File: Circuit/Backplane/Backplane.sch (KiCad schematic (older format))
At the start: 51 parts

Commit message: fixground
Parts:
- removed R?: 4.7K, symbol R
- added R?: 4.7K, symbol R
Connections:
- net GND: now also R?.2
- net at U?.17 (TEST): now also R?.1
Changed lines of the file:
@@
 $EndDescr
-$Comp
-L TUSB4041I U?
-U 1 1 5A564068
-P 4400 4650
-F 0 "U?" H 5000 6750 50  0000 L CNN
-F 1 "TUSB4041I" H 5000 6650 50  0000 L CNN
-F 2 "Housings_QFP:HTQFP-64_1EP_10x10mm_Pitch0.5mm_ThermalPad" H 5600 6650 50  0001 L CNN
-F 3 "" H 4100 4850 50  0001 C CNN
-	1    4400 4650
-	1    0    0    -1
-$EndComp
 $Comp
 L Conn-PCIE-x1 CON?
@@
 $EndComp
 $Comp
-L R R?
-U 1 1 5A56456F
-P 2550 6700
-F 0 "R?" V 2630 6700 50  0000 C CNN
-F 1 "4.7K" V 2550 6700 50  0000 C CNN
-F 2 "" V 2480 6700 50  0001 C CNN
-F 3 "" H 2550 6700 50  0001 C CNN
-	1    2550 6700
-	1    0    0    -1
-$EndComp
-$Comp
-L GND #PWR?
-U 1 1 5A564784
-P 3250 6900
-F 0 "#PWR?" H 3250 6650 50  0001 C CNN
-F 1 "GND" H 3250 6750 50  0000 C CNN
-F 2 "" H 3250 6900 50  0001 C CNN
-F 3 "" H 3250 6900 50  0001 C CNN
-	1    3250 6900
-	1    0    0    -1
-$EndComp
-$Comp
 L USB_OTG J?
 U 1 1 5A564864
@@
 	7250 5850 6700 5850
 Wire Wire Line
-	4400 6900 4400 6750
-Connection ~ 3250 6900
-Wire Wire Line
 	2100 3550 2950 3550
 Wire Wire Line
@@
 Wire Wire Line
 	1950 6250 3100 6250
-Wire Wire Line
-	3100 6450 2550 6450
-Wire Wire Line
-	2550 6450 2550 6550
-Wire Wire Line
-	2550 6850 2550 6900
-Connection ~ 2550 6900
 $Comp
 L R R?
@@
 	1    0    0    -1
 $EndComp
-Wire Wire Line
-	2550 6900 4400 6900
+$Comp
+L R R?
+U 1 1 5A6197DD
+P 2850 6450
+F 0 "R?" V 2930 6450 50  0000 C CNN
+F 1 "4.7K" V 2850 6450 50  0000 C CNN
+F 2 "" V 2780 6450 50  0001 C CNN
+F 3 "" H 2850 6450 50  0001 C CNN
+	1    2850 6450
+	0    1    1    0
+$EndComp
+Wire Wire Line
+	3100 6450 3000 6450
+Wire Wire Line
+	2700 6450 2700 6750
+$Comp
+L GND #PWR?
+U 1 1 5A619BE9
+P 3500 6750
+F 0 "#PWR?" H 3500 6500 50  0001 C CNN
+F 1 "GND" H 3500 6600 50  0000 C CNN
+F 2 "" H 3500 6750 50  0001 C CNN
+F 3 "" H 3500 6750 50  0001 C CNN
+	1    3500 6750
+	1    0    0    -1
+$EndComp
+$Comp
+L TUSB4041I U?
+U 1 1 5A564068
+P 4400 4650
+F 0 "U?" H 5000 6750 50  0000 L CNN
+F 1 "TUSB4041I" H 5000 6650 50  0000 L CNN
+F 2 "Housings_QFP:HTQFP-64_1EP_10x10mm_Pitch0.5mm_ThermalPad" H 5600 6650 50  0001 L CNN
+F 3 "" H 4100 4850 50  0001 C CNN
+	1    4400 4650
+	1    0    0    -1
+$EndComp
+Wire Wire Line
+	2700 6750 4400 6750
+Connection ~ 3500 6750
 $EndSCHEMATC

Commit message: PcieFix
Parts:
- removed P?: InnerPoe, symbol XT30
- CON?: value Conn-PCIE-x1 -> Power_dist
- CON?: value Conn-PCIE-x1 -> Peripheral_bridge
- J?: value PressureSensor -> Pneumatic
- P?: value General1 -> Computer1
- P?: value General2 -> Computer2
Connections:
- net 12V: no longer CON?.A3 (V12), P?.1 (P1), P?.1 (P1)
- net GND: no longer CON?.B7 (GND), J?.1 (Pin_1)
- net VPCIE: now also P?.1 (P1)
- net at CON?.A7 (JTAG_TDO): no longer J?.2 (Pin_2)
- net at CON?.A8 (JTAG_TMS): no longer J?.3 (Pin_3)
- net Vin: no longer names the net of C?.1, CON?.A10 (VCC3), CON?.A9 (VCC3), CON?.B8 (VCC3), L?.1
- new net GND_Vbatt: CON?.B7 (GND)
- new net Vbatt: CON?.A3 (V12), P?.1 (P1)
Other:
- moved on the sheet: J?
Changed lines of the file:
@@
 P 7400 1550
 F 0 "CON?" H 7550 1600 60  0000 C CNN
-F 1 "Conn-PCIE-x1" H 7800 -550 60  0000 C CNN
+F 1 "Power_dist" H 7800 -550 60  0000 C CNN
 F 2 "" H 7400 1550 60  0001 C CNN
 F 3 "" H 7400 1550 60  0001 C CNN
@@
 P 7450 4250
 F 0 "CON?" H 7600 4300 60  0000 C CNN
-F 1 "Conn-PCIE-x1" H 7850 2150 60  0000 C CNN
+F 1 "Peripheral_bridge" H 7850 2150 60  0000 C CNN
 F 2 "" H 7450 4250 60  0001 C CNN
 F 3 "" H 7450 4250 60  0001 C CNN
@@
 Text GLabel 8500 4500 2    60   Input ~ 0
 12V
-Text GLabel 8450 1800 2    60   Input ~ 0
-12V
 $Comp
 L C C?
@@
 Text GLabel 8450 2500 2    60   Input ~ 0
 VPCIE
-Text GLabel 7150 5050 0    60   Input ~ 0
-Vin
-Text GLabel 8500 5200 2    60   Input ~ 0
-Vin
 $Comp
 L C C?
@@
 Text GLabel 5750 5050 0    60   Input ~ 0
 5V
-Text GLabel 6450 5050 2    60   Input ~ 0
-Vin
-$Comp
-L XT30 P?
-U 1 1 5A58183A
-P 10450 2000
-F 0 "P?" H 10450 2150 50  0000 C CNN
-F 1 "InnerPoe" H 10450 1850 50  0000 C CNN
-F 2 "" H 10450 2000 60  0000 C CNN
-F 3 "" H 10450 2000 60  0000 C CNN
-	1    10450 2000
-	1    0    0    -1
-$EndComp
 $Comp
 L XT30 P?
@@
 P 10450 3200
 F 0 "P?" H 10450 3350 50  0000 C CNN
-F 1 "General1" H 10450 3050 50  0000 C CNN
+F 1 "Computer1" H 10450 3050 50  0000 C CNN
 F 2 "" H 10450 3200 60  0000 C CNN
 F 3 "" H 10450 3200 60  0000 C CNN
@@
 P 10450 3600
 F 0 "P?" H 10450 3750 50  0000 C CNN
-F 1 "General2" H 10450 3450 50  0000 C CNN
+F 1 "Computer2" H 10450 3450 50  0000 C CNN
 F 2 "" H 10450 3600 60  0000 C CNN
 F 3 "" H 10450 3600 60  0000 C CNN
 	1    10450 3600
-	1    0    0    -1
-$EndComp
-$Comp
-L GND #PWR?
-U 1 1 5A58301B
-P 10150 2100
-F 0 "#PWR?" H 10150 1850 50  0001 C CNN
-F 1 "GND" H 10150 1950 50  0000 C CNN
-F 2 "" H 10150 2100 50  0001 C CNN
-F 3 "" H 10150 2100 50  0001 C CNN
-	1    10150 2100
 	1    0    0    -1
 $EndComp
@@
 	1    0    0    -1
 $EndComp
-Text GLabel 10150 1950 0    60   Input ~ 0
-12V
-Text GLabel 10150 2350 0    60   Input ~ 0
-12V
 Text GLabel 10150 3150 0    60   Input ~ 0
 12V
@@
 L Conn_01x03 J?
 U 1 1 5A584C3E
-P 9550 2050
-F 0 "J?" H 9550 2250 50  0000 C CNN
-F 1 "Rs232DVL" H 9550 1850 50  0000 C CNN
-F 2 "" H 9550 2050 50  0001 C CNN
-F 3 "" H 9550 2050 50  0001 C CNN
-	1    9550 2050
-	1    0    0    -1
-$EndComp
-Text GLabel 10150 2750 0    60   Input ~ 0
-12V
+P 9550 4250
+F 0 "J?" H 9550 4450 50  0000 C CNN
+F 1 "Rs232DVL" H 9550 4050 50  0000 C CNN
+F 2 "" H 9550 4250 50  0001 C CNN
+F 3 "" H 9550 4250 50  0001 C CNN
+	1    9550 4250
+	1    0    0    -1
+$EndComp
 $Comp
 L Conn_01x03 J?
@@
 Connection ~ 7200 1750
 Wire Wire Line
-	8350 1750 8350 1850
-Wire Wire Line
 	7200 1950 7150 1950
 Wire Wire Line
 	7150 1950 7150 3700
 Wire Wire Line
-	7150 2250 7200 2250
-Wire Wire Line
 	7150 2950 7200 2950
-Connection ~ 7150 2250
 Wire Wire Line
 	7150 3250 7200 3250
@@
 	7150 3450 7200 3450
 Connection ~ 7150 3250
-Wire Wire Line
-	8350 1950 9350 1950
 Wire Wire Line
 	8400 2850 8350 2850
@@
 	7200 1750 7100 1750
 Wire Wire Line
-	8350 1800 8450 1800
-Connection ~ 8350 1800
-Wire Wire Line
 	7250 4450 7150 4450
 Wire Wire Line
@@
 Connection ~ 6550 2550
 Wire Wire Line
-	7250 5050 7150 5050
+	6050 5050 7250 5050
 Wire Wire Line
 	8400 5150 8400 5250
-Wire Wire Line
-	8400 5200 8500 5200
-Connection ~ 8400 5200
 Connection ~ 6300 5050
 Wire Wire Line
@@
 	7150 3700 8400 3700
 Wire Wire Line
-	10250 1950 10150 1950
-Wire Wire Line
-	10250 2050 10150 2050
-Wire Wire Line
-	10150 2050 10150 2100
-Wire Wire Line
 	10250 2350 10150 2350
 Wire Wire Line
@@
 Wire Wire Line
 	10150 3650 10150 3700
-Connection ~ 8400 1950
-Wire Wire Line
-	8350 2250 8450 2250
-Wire Wire Line
-	8450 2250 8450 2050
-Wire Wire Line
-	8450 2050 9350 2050
-Wire Wire Line
-	8500 2150 9350 2150
-Wire Wire Line
-	8500 2150 8500 2350
-Wire Wire Line
-	8500 2350 8350 2350
 Wire Wire Line
 	6850 4950 7250 4950
@@
 	0    1    1    0
 $EndComp
-Wire Wire Line
-	6050 5050 6450 5050
 $Comp
 L Ferrite_Bead L?
@@
 P 9600 5400
 F 0 "J?" H 9650 5600 50  0000 C CNN
-F 1 "PressureSensor" H 9650 5100 50  0000 C CNN
+F 1 "Pneumatic" H 9650 5100 50  0000 C CNN
 F 2 "" H 9600 5400 50  0001 C CNN
 F 3 "" H 9600 5400 50  0001 C CNN
@@
 	2700 6750 4400 6750
 Connection ~ 3500 6750
+Wire Wire Line
+	8350 1750 8500 1750
+Wire Wire Line
+	8500 1750 8500 1650
+Wire Wire Line
+	8500 1650 8650 1650
+Wire Wire Line
+	8350 1850 8650 1850
+Text GLabel 8650 1650 2    60   Input ~ 0
+12V
+Text GLabel 8650 1850 2    60   Input ~ 0
+Vbatt
+Wire Wire Line
+	7200 2250 6800 2250
+Wire Wire Line
+	6800 2250 6800 1450
+Wire Wire Line
+	6800 1450 6850 1450
+Text GLabel 6850 1450 2    60   Input ~ 0
+GND_Vbatt
+Text GLabel 10150 2350 0    60   Input ~ 0
+VPCIE
+Text GLabel 10150 2750 0    60   Input ~ 0
+Vbatt
+Wire Wire Line
+	8400 1950 8350 1950
+Wire Wire Line
+	8400 5200 8550 5200
+Wire Wire Line
+	8550 5200 8550 6600
+Wire Wire Line
+	8550 6600 6550 6600
+Wire Wire Line
+	6550 6600 6550 5050
+Connection ~ 6550 5050
+Connection ~ 8400 5200
 $EndSCHEMATC

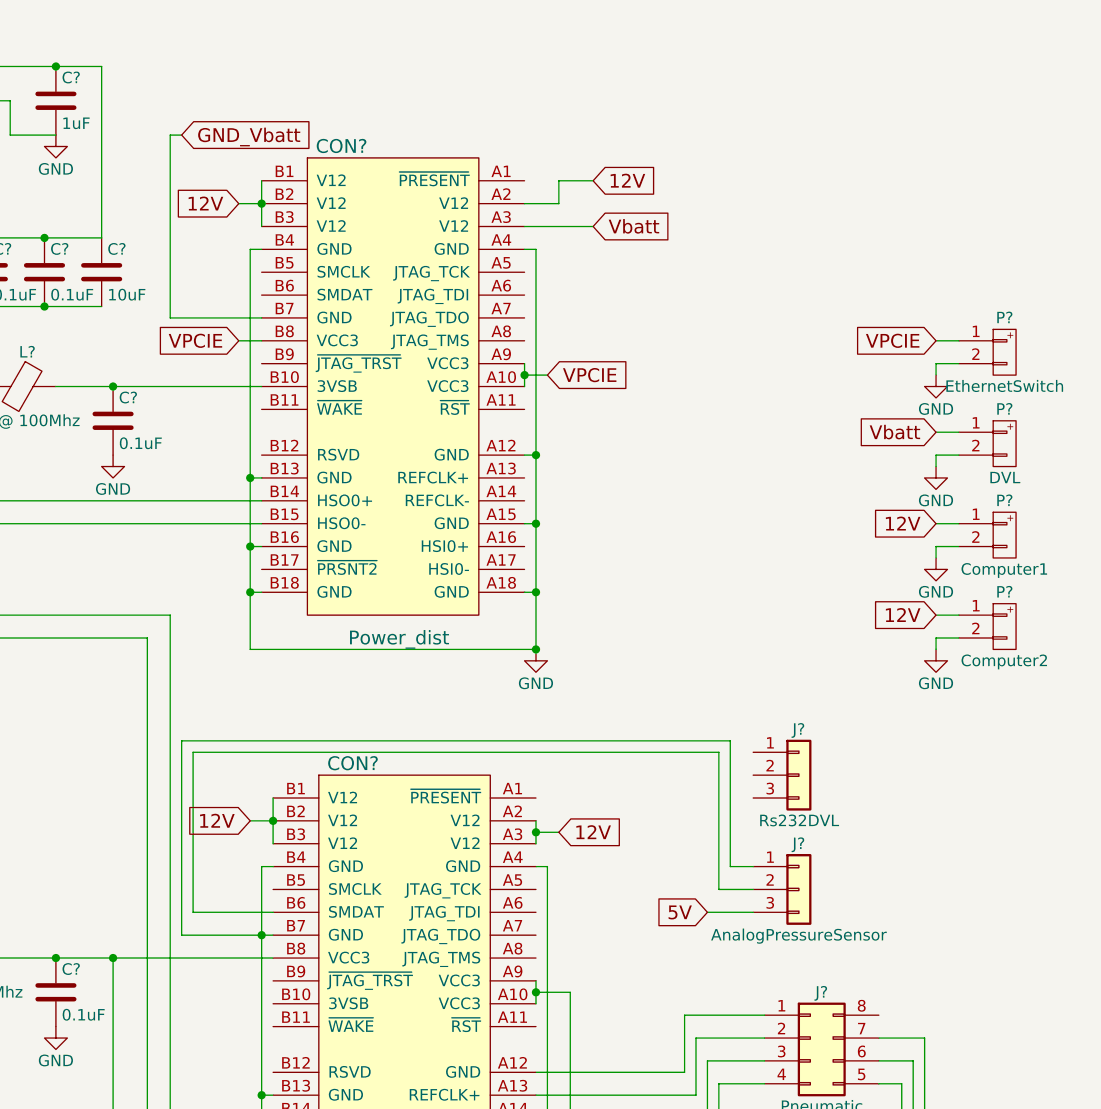
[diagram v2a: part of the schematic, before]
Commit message: fixDv,Change_label_to_powerflag
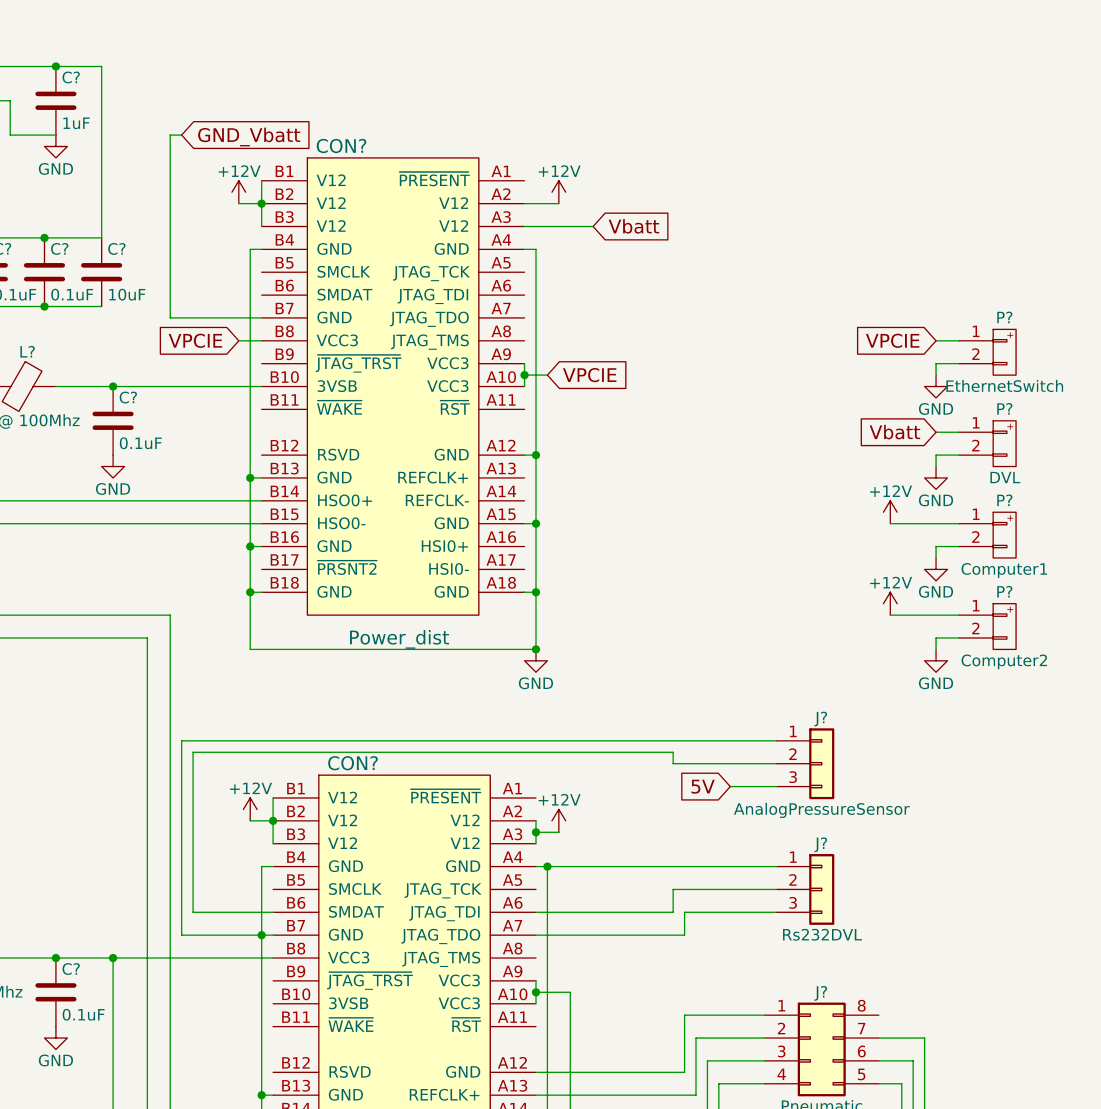
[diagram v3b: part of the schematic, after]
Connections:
- net GND: now also J?.1 (Pin_1)
- net at CON?.A6 (JTAG_TDI): now also J?.2 (Pin_2)
- net at CON?.A7 (JTAG_TDO): now also J?.3 (Pin_3)
- net 12V renamed +12V
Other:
- moved on the sheet: J?
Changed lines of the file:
@@
 	1    0    0    -1
 $EndComp
-Text GLabel 7100 1750 0    60   Input ~ 0
-12V
-Text GLabel 7150 4450 0    60   Input ~ 0
-12V
-Text GLabel 8500 4500 2    60   Input ~ 0
-12V
 $Comp
 L C C?
@@
 	1    0    0    -1
 $EndComp
-Text GLabel 10150 3150 0    60   Input ~ 0
-12V
-Text GLabel 10150 3550 0    60   Input ~ 0
-12V
 $Comp
 L Conn_01x03 J?
 U 1 1 5A584C3E
-P 9550 4250
-F 0 "J?" H 9550 4450 50  0000 C CNN
-F 1 "Rs232DVL" H 9550 4050 50  0000 C CNN
-F 2 "" H 9550 4250 50  0001 C CNN
-F 3 "" H 9550 4250 50  0001 C CNN
-	1    9550 4250
+P 9650 4750
+F 0 "J?" H 9650 4950 50  0000 C CNN
+F 1 "Rs232DVL" H 9650 4550 50  0000 C CNN
+F 2 "" H 9650 4750 50  0001 C CNN
+F 3 "" H 9650 4750 50  0001 C CNN
+	1    9650 4750
 	1    0    0    -1
 $EndComp
@@
 L Conn_01x03 J?
 U 1 1 5A5725F7
-P 9550 4750
-F 0 "J?" H 9550 4950 50  0000 C CNN
-F 1 "AnalogPressureSensor" H 9550 4550 50  0000 C CNN
-F 2 "" H 9550 4750 50  0001 C CNN
-F 3 "" H 9550 4750 50  0001 C CNN
-	1    9550 4750
-	1    0    0    -1
-$EndComp
-Text GLabel 9150 4850 0    60   Input ~ 0
+P 9650 4200
+F 0 "J?" H 9650 4400 50  0000 C CNN
+F 1 "AnalogPressureSensor" H 9650 4000 50  0000 C CNN
+F 2 "" H 9650 4200 50  0001 C CNN
+F 3 "" H 9650 4200 50  0001 C CNN
+	1    9650 4200
+	1    0    0    -1
+$EndComp
+Text GLabel 9250 4300 0    60   Input ~ 0
 5V
 $Comp
@@
 Connection ~ 7200 5950
 Wire Wire Line
-	8400 4650 8450 4650
+	8400 4650 9450 4650
 Wire Wire Line
 	8400 5550 9050 5550
@@
 	10150 2850 10150 2900
 Wire Wire Line
-	10250 3150 10150 3150
+	9950 3150 10250 3150
 Wire Wire Line
 	10250 3250 10150 3250
@@
 	10150 3250 10150 3300
 Wire Wire Line
-	10250 3550 10150 3550
+	9950 3550 10250 3550
 Wire Wire Line
 	10250 3650 10150 3650
@@
 	6850 4950 6850 4100
 Wire Wire Line
-	6850 4100 9250 4100
-Wire Wire Line
-	9250 4100 9250 4650
-Wire Wire Line
-	9250 4650 9350 4650
+	6850 4100 9450 4100
 Wire Wire Line
 	7250 4850 6900 4850
@@
 	6900 4850 6900 4150
 Wire Wire Line
-	6900 4150 9200 4150
-Wire Wire Line
-	9200 4150 9200 4750
-Wire Wire Line
-	9200 4750 9350 4750
-Wire Wire Line
-	9350 4850 9150 4850
+	9450 4300 9250 4300
 Wire Wire Line
 	8400 3700 8400 1950
@@
 	8350 1750 8500 1750
 Wire Wire Line
-	8500 1750 8500 1650
-Wire Wire Line
-	8500 1650 8650 1650
-Wire Wire Line
 	8350 1850 8650 1850
-Text GLabel 8650 1650 2    60   Input ~ 0
-12V
 Text GLabel 8650 1850 2    60   Input ~ 0
 Vbatt
@@
 Connection ~ 6550 5050
 Connection ~ 8400 5200
+Connection ~ 8450 4650
+Wire Wire Line
+	8400 4950 9050 4950
+Wire Wire Line
+	9050 4950 9050 4850
+Wire Wire Line
+	9050 4850 9450 4850
+Wire Wire Line
+	8400 4850 9000 4850
+Wire Wire Line
+	9000 4850 9000 4750
+Wire Wire Line
+	9000 4750 9450 4750
+Wire Wire Line
+	6900 4150 9000 4150
+Wire Wire Line
+	9000 4150 9000 4200
+Wire Wire Line
+	9000 4200 9450 4200
+$Comp
+L +12V #PWR?
+U 1 1 5A60ECE0
+P 7100 1750
+F 0 "#PWR?" H 7100 1600 50  0001 C CNN
+F 1 "+12V" H 7100 1890 50  0000 C CNN
+F 2 "" H 7100 1750 50  0001 C CNN
+F 3 "" H 7100 1750 50  0001 C CNN
+	1    7100 1750
+	1    0    0    -1
+$EndComp
+$Comp
+L +12V #PWR?
+U 1 1 5A60EF7F
+P 8500 1750
+F 0 "#PWR?" H 8500 1600 50  0001 C CNN
+F 1 "+12V" H 8500 1890 50  0000 C CNN
+F 2 "" H 8500 1750 50  0001 C CNN
+F 3 "" H 8500 1750 50  0001 C CNN
+	1    8500 1750
+	1    0    0    -1
+$EndComp
+$Comp
+L +12V #PWR?
+U 1 1 5A60F4A5
+P 9950 3150
+F 0 "#PWR?" H 9950 3000 50  0001 C CNN
+F 1 "+12V" H 9950 3290 50  0000 C CNN
+F 2 "" H 9950 3150 50  0001 C CNN
+F 3 "" H 9950 3150 50  0001 C CNN
+	1    9950 3150
+	1    0    0    -1
+$EndComp
+$Comp
+L +12V #PWR?
+U 1 1 5A60F51D
+P 9950 3550
+F 0 "#PWR?" H 9950 3400 50  0001 C CNN
+F 1 "+12V" H 9950 3690 50  0000 C CNN
+F 2 "" H 9950 3550 50  0001 C CNN
+F 3 "" H 9950 3550 50  0001 C CNN
+	1    9950 3550
+	1    0    0    -1
+$EndComp
+$Comp
+L +12V #PWR?
+U 1 1 5A60FB3B
+P 8500 4500
+F 0 "#PWR?" H 8500 4350 50  0001 C CNN
+F 1 "+12V" H 8500 4640 50  0000 C CNN
+F 2 "" H 8500 4500 50  0001 C CNN
+F 3 "" H 8500 4500 50  0001 C CNN
+	1    8500 4500
+	1    0    0    -1
+$EndComp
+$Comp
+L +12V #PWR?
+U 1 1 5A60FBB3
+P 7150 4450
+F 0 "#PWR?" H 7150 4300 50  0001 C CNN
+F 1 "+12V" H 7150 4590 50  0000 C CNN
+F 2 "" H 7150 4450 50  0001 C CNN
+F 3 "" H 7150 4450 50  0001 C CNN
+	1    7150 4450
+	1    0    0    -1
+$EndComp
 $EndSCHEMATC

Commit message: 5Vlabel_to_flag
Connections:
- net 5V renamed +5V
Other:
- moved on the sheet: C?, CON?, J?, L?, P?, R?, U?, Y?
